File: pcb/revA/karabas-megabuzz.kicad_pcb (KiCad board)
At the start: 4 copper layers, 92.2 x 44 mm, 177 parts, among them J1 FPGA JTAG, J2 Conn_02x30_Row_Letter_First, J3 PJ307, J4 Conn_01x04, J5 5VP, SW1 SW_DIP_x05, U1 XC6SLX25-FTG256, U10 PCM5102A, U11 PCM1808PWR, U12 CY62167EV30LL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

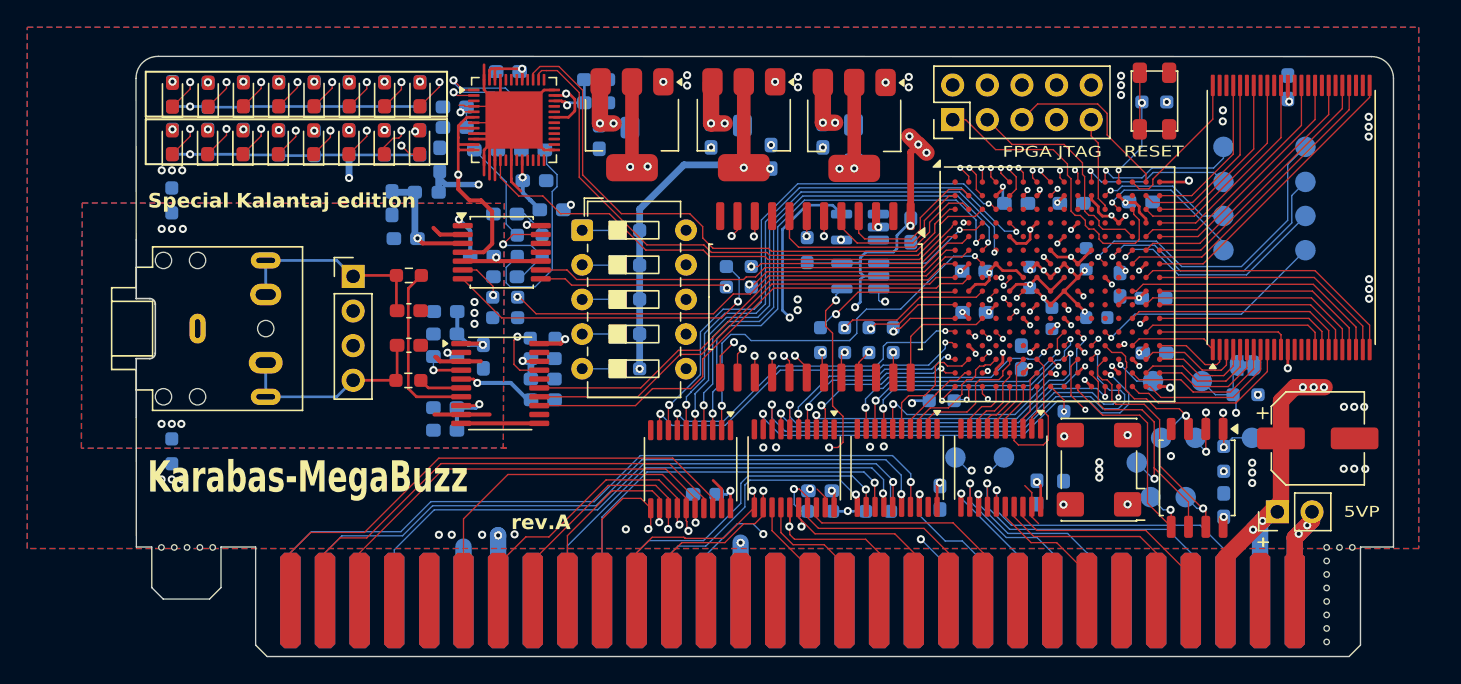
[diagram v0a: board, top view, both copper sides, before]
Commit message: Updated revA - rerouted OPL3 reset to /MIDI_RST
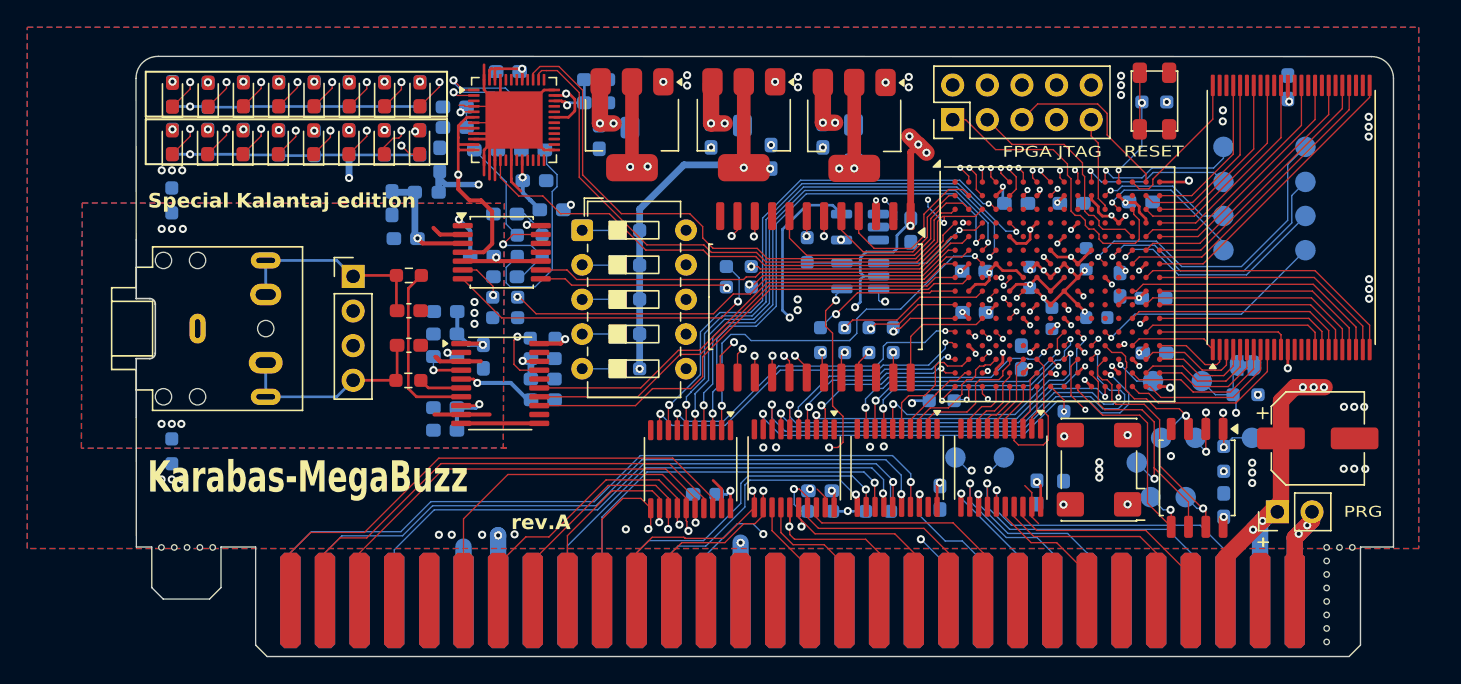
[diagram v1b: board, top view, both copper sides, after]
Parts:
- J5: value 5VP -> PRG
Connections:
- U8 pad 3: ~{RST} -> ~{MIDI_RST}
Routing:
- net ~{MIDI_RST}: track 44.1 -> 53.1 mm, vias 0 -> 3
- net ~{RST}: track 37.2 -> 42.9 mm
- net xD0: track 39.4 -> 40.7 mm
- net +1V2: track 47.1 -> 48.2 mm
- net YM_A1: track 11.5 -> 12.6 mm
- net YM_A0: track 11.7 -> 12.7 mm
- net MIDI_CLK: track 43.0 -> 44.0 mm
- net ~{YM_CS}: track 17.0 -> 17.9 mm
- net +5V: track 172.7 -> 173.6 mm
- net MIDI_IN: track 38.3 -> 38.8 mm
- net xA13: track 36.7 -> 37.3 mm

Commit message: Removed polygons under BGA chip on F.Cu layer
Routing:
- net GND: track 120.8 -> 127.0 mm, vias 84 -> 85

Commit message: Updated revA (cosmetic changes)
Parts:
- BTN1: value RESET -> Reset
- D1: value L0 -> BLUE
- D10: value R1 -> GREEN
- D11: value R2 -> GREEN
- D12: value R3 -> GREEN
- D13: value R4 -> GREEN
- D14: value R5 -> YELLOW
- D15: value R6 -> YELLOW
- D16: value R7 -> RED
- D2: value L1 -> GREEN
- D3: value L2 -> GREEN
- D4: value L3 -> GREEN
- D5: value L4 -> GREEN
- D6: value L5 -> YELLOW
- D7: value L6 -> YELLOW
- D8: value L7 -> RED
- D9: value R0 -> BLUE
- J5: value PRG -> 5V_PRG
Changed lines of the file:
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@@
 			)
 		)
-		(property "Value" "L0"
+		(property "Value" "BLUE"
 			(at 0 1.43 90)
 			(layer "F.Fab")
@@
 			)
 		)
-		(property "Value" "R3"
+		(property "Value" "GREEN"
 			(at 0 1.43 90)
 			(layer "F.Fab")
@@
 			)
 		)
-		(property "Value" "L5"
+		(property "Value" "YELLOW"
 			(at 0 1.43 90)
 			(layer "F.Fab")
@@
 			)
 		)
-		(property "Value" "R0"
+		(property "Value" "BLUE"
 			(at 0 1.43 90)
 			(layer "F.Fab")
@@
 			)
 		)
-		(attr through_hole)
+		(attr through_hole exclude_from_bom dnp)
 		(duplicate_pad_numbers_are_jumpers no)
 		(fp_line
@@
 			)
 		)
-		(property "Value" "L4"
+		(property "Value" "GREEN"
 			(at 0 1.43 90)
 			(layer "F.Fab")
@@
 			)
 		)
-		(property "Value" "R5"
+		(property "Value" "YELLOW"
 			(at 0 1.43 90)
 			(layer "F.Fab")
@@
 			)
 		)
-		(property "Value" "L1"
+		(property "Value" "GREEN"
 			(at 0 1.43 90)
 			(layer "F.Fab")
@@
 			)
 		)
-		(property "Value" "L6"
+		(property "Value" "YELLOW"
 			(at 0 1.43 90)
 			(layer "F.Fab")
@@
 			)
 		)
-		(property "Value" "L3"
+		(property "Value" "GREEN"
 			(at 0 1.43 90)
 			(layer "F.Fab")
@@
 			)
 		)
-		(property "Value" "R4"
+		(property "Value" "GREEN"
 			(at 0 1.43 90)
 			(layer "F.Fab")
@@
 			)
 		)
-		(property "Value" "L7"
+		(property "Value" "RED"
 			(at 0 1.43 90)
 			(layer "F.Fab")
@@
 			)
 		)
-		(attr through_hole)
+		(attr through_hole exclude_from_bom dnp)
 		(duplicate_pad_numbers_are_jumpers no)
 		(fp_line
@@
 			)
 		)
-		(property "Value" "R2"
+		(property "Value" "GREEN"
 			(at 0 1.43 90)
 			(layer "F.Fab")
@@
 			)
 		)
-		(property "Value" "R6"
+		(property "Value" "YELLOW"
 			(at 0 1.43 90)
 			(layer "F.Fab")
@@
 			)
 		)
-		(property "Value" "PRG"
+		(property "Value" "5V_PRG"
 			(at 0.01 4.865 180)
 			(layer "F.SilkS" knockout)
@@
 			)
 		)
-		(attr through_hole exclude_from_bom)
+		(attr through_hole exclude_from_bom dnp)
 		(duplicate_pad_numbers_are_jumpers no)
 		(fp_line
@@
 			)
 		)
-		(property "Value" "RESET"
+		(property "Value" "Reset"
 			(at -3.7 -2.25 180)
 			(layer "F.SilkS" knockout)
@@
 			)
 		)
-		(property "Value" "R1"
+		(property "Value" "GREEN"
 			(at 0 1.43 90)
 			(layer "F.Fab")
@@
 			)
 		)
-		(property "Value" "R7"
+		(property "Value" "RED"
 			(at 0 1.43 90)
 			(layer "F.Fab")
@@
 			)
 		)
-		(property "Value" "L2"
+		(property "Value" "GREEN"
 			(at 0 1.43 90)
 			(layer "F.Fab")
@@
 			)
 		)
+		(attr exclude_from_bom)
 		(duplicate_pad_numbers_are_jumpers no)
 		(fp_circle
@@
 			)
 		)
-		(attr smd)
+		(attr smd exclude_from_bom dnp)
 		(duplicate_pad_numbers_are_jumpers no)
 		(fp_line
@@
 			)
 		)
+		(attr exclude_from_bom)
 		(duplicate_pad_numbers_are_jumpers no)
 		(fp_circle
@@
 			)
 		)
+		(attr exclude_from_bom)
 		(duplicate_pad_numbers_are_jumpers no)
 		(fp_circle
@@
 			)
 		)
+		(attr exclude_from_bom)
 		(duplicate_pad_numbers_are_jumpers no)
 		(fp_circle
@@
 			)
 		)
+		(attr exclude_from_bom)
 		(duplicate_pad_numbers_are_jumpers no)
 		(fp_circle
@@
 			)
 		)
+		(attr exclude_from_bom)
 		(duplicate_pad_numbers_are_jumpers no)
 		(fp_circle
@@
 			)
 		)
+		(attr exclude_from_bom)
 		(duplicate_pad_numbers_are_jumpers no)
 		(fp_circle
@@
 			)
 		)
+		(attr exclude_from_bom)
 		(duplicate_pad_numbers_are_jumpers no)
 		(fp_circle
@@
 			)
 		)
-		(attr smd)
+		(attr smd exclude_from_bom dnp)
 		(duplicate_pad_numbers_are_jumpers no)
 		(fp_line
@@
 		)
 		(zone_connect 1)
-		(attr allow_soldermask_bridges)
+		(attr exclude_from_bom allow_soldermask_bridges)
 		(net_tie_pad_groups "1, 2")
 		(duplicate_pad_numbers_are_jumpers no)
@@
 			)
 		)
+		(attr exclude_from_bom)
 		(duplicate_pad_numbers_are_jumpers no)
 		(fp_circle
@@
 			)
 		)
+		(attr exclude_from_bom)
 		(duplicate_pad_numbers_are_jumpers no)
 		(fp_circle
@@
 			)
 		)
+		(attr exclude_from_bom)
 		(duplicate_pad_numbers_are_jumpers no)
 		(fp_circle
@@
 			)
 		)
+		(attr exclude_from_bom)
 		(duplicate_pad_numbers_are_jumpers no)
 		(fp_circle
@@
 			)
 		)
+		(attr exclude_from_bom)
 		(duplicate_pad_numbers_are_jumpers no)
 		(fp_circle
@@
 			)
 		)
+		(attr exclude_from_bom)
 		(duplicate_pad_numbers_are_jumpers no)
 		(fp_circle
@@
 			)
 		)
+		(attr exclude_from_bom)
 		(duplicate_pad_numbers_are_jumpers no)
 		(fp_circle
@@
 			)
 		)
+		(attr exclude_from_bom)
 		(duplicate_pad_numbers_are_jumpers no)
 		(fp_circle
@@
 			)
 		)
+		(attr exclude_from_bom)
 		(duplicate_pad_numbers_are_jumpers no)
 		(fp_circle
@@
 			)
 		)
+		(attr exclude_from_bom)
 		(duplicate_pad_numbers_are_jumpers no)
 		(fp_circle
